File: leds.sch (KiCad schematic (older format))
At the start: 0 parts

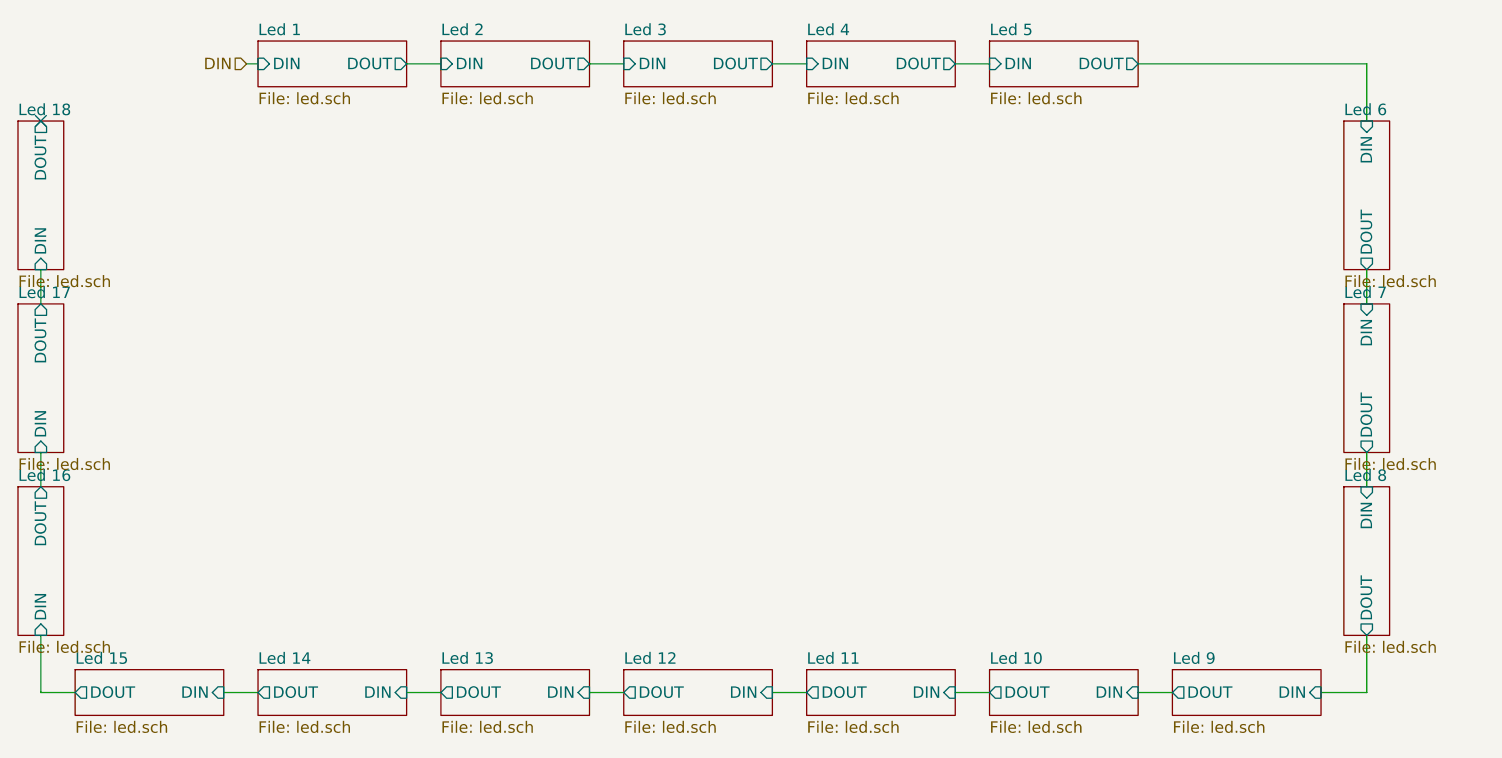
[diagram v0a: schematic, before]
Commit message: Place and route WS2812 LEDs
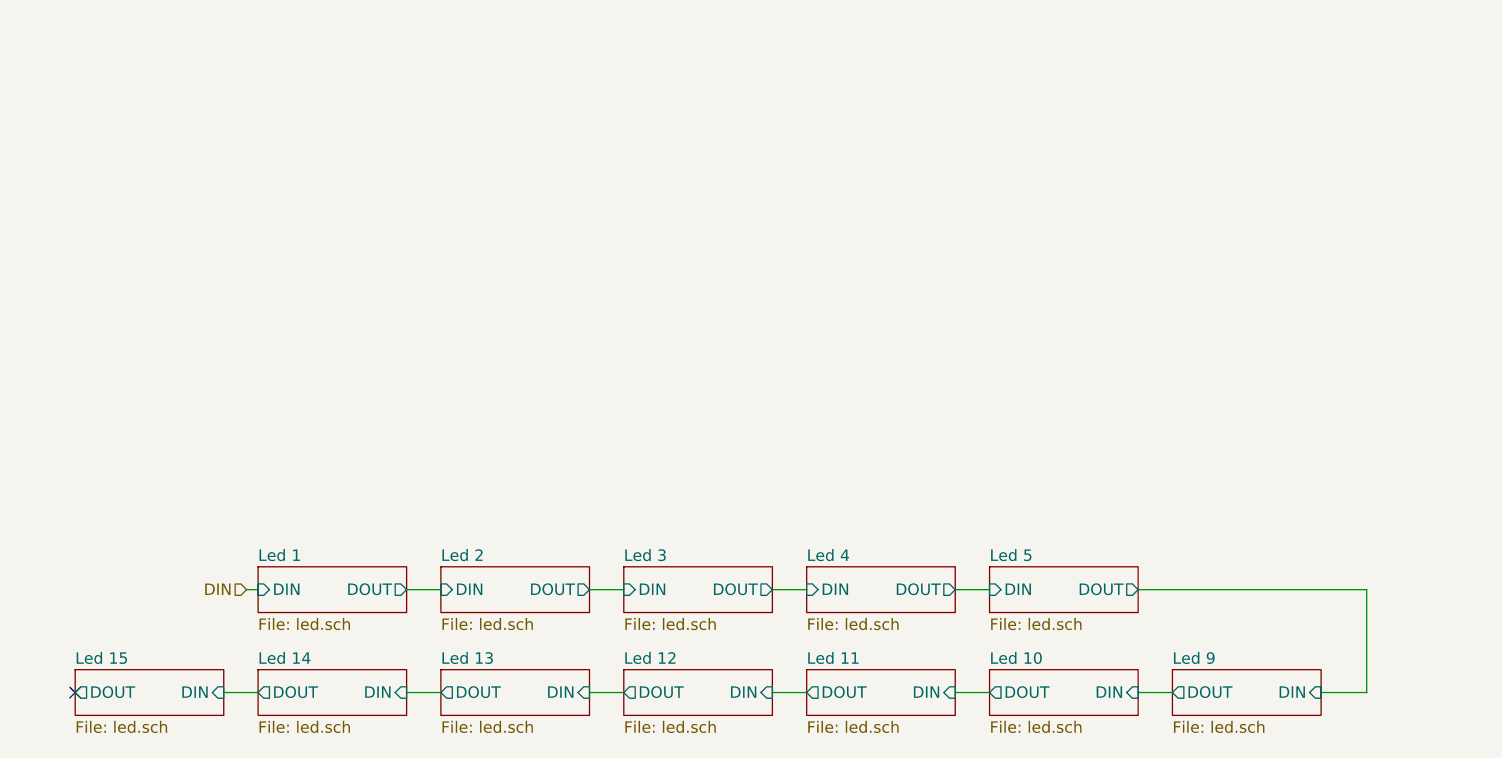
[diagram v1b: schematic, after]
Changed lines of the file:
@@
 $Descr A4 11693 8268
 encoding utf-8
-Sheet 5 23
+Sheet 5 17
 Title ""
 Date ""
@@
 Comment4 ""
 $EndDescr
-Text HLabel 2450 2200 0    50   Input ~ 0
+Text HLabel 2450 4500 0    50   Input ~ 0
 DIN
-$Sheet
-S 7250 2450 200  650
-U 620616BF
-F0 "Led 6" 50
-F1 "led.sch" 50
-F2 "DIN" I T 7350 2450 50
-F3 "DOUT" O B 7350 3100 50
-$EndSheet
-Wire Wire Line
-	7350 3100 7350 3250
-Wire Wire Line
-	7350 2450 7350 2200
-$Sheet
-S 7250 3250 200  650
-U 6206183F
-F0 "Led 7" 50
-F1 "led.sch" 50
-F2 "DIN" I T 7350 3250 50
-F3 "DOUT" O B 7350 3900 50
-$EndSheet
-Wire Wire Line
-	7350 3900 7350 4050
-$Sheet
-S 7250 4050 200  650
-U 62061912
-F0 "Led 8" 50
-F1 "led.sch" 50
-F2 "DIN" I T 7350 4050 50
-F3 "DOUT" O B 7350 4700 50
-$EndSheet
 $Sheet
 S 6500 4850 650  200
@@
 Wire Wire Line
 	7150 4950 7350 4950
-Wire Wire Line
-	7350 4700 7350 4950
 Wire Wire Line
 	5700 4950 5550 4950
@@
 F3 "DOUT" O L 1700 4950 50
 $EndSheet
-Wire Wire Line
-	1700 4950 1550 4950
-$Sheet
-S 1450 4050 200  650
-U 62062FE6
-F0 "Led 16" 50
-F1 "led.sch" 50
-F2 "DIN" I B 1550 4700 50
-F3 "DOUT" O T 1550 4050 50
-$EndSheet
-Wire Wire Line
-	1550 4050 1550 3900
-Wire Wire Line
-	1550 4700 1550 4950
-$Sheet
-S 1450 3250 200  650
-U 62063495
-F0 "Led 17" 50
-F1 "led.sch" 50
-F2 "DIN" I B 1550 3900 50
-F3 "DOUT" O T 1550 3250 50
-$EndSheet
-Wire Wire Line
-	1550 3250 1550 3100
-$Sheet
-S 1450 2450 200  650
-U 620637A1
-F0 "Led 18" 50
-F1 "led.sch" 50
-F2 "DIN" I B 1550 3100 50
-F3 "DOUT" O T 1550 2450 50
-$EndSheet
-NoConn ~ 1550 2450
 $Sheet
 S 5700 4850 650  200
@@
 $EndSheet
 $Sheet
-S 5700 2100 650  200
+S 5700 4400 650  200
 U 62060D3F
 F0 "Led 5" 50
 F1 "led.sch" 50
-F2 "DIN" I L 5700 2200 50
-F3 "DOUT" O R 6350 2200 50
+F2 "DIN" I L 5700 4500 50
+F3 "DOUT" O R 6350 4500 50
 $EndSheet
 Wire Wire Line
-	5550 2200 5700 2200
+	5550 4500 5700 4500
 $Sheet
-S 4900 2100 650  200
+S 4900 4400 650  200
 U 62060CAF
 F0 "Led 4" 50
 F1 "led.sch" 50
-F2 "DIN" I L 4900 2200 50
-F3 "DOUT" O R 5550 2200 50
+F2 "DIN" I L 4900 4500 50
+F3 "DOUT" O R 5550 4500 50
 $EndSheet
 Wire Wire Line
-	4750 2200 4900 2200
+	4750 4500 4900 4500
 $Sheet
-S 4100 2100 650  200
+S 4100 4400 650  200
 U 62060C37
 F0 "Led 3" 50
 F1 "led.sch" 50
-F2 "DIN" I L 4100 2200 50
-F3 "DOUT" O R 4750 2200 50
+F2 "DIN" I L 4100 4500 50
+F3 "DOUT" O R 4750 4500 50
 $EndSheet
 Wire Wire Line
-	3950 2200 4100 2200
+	3950 4500 4100 4500
 $Sheet
-S 3300 2100 650  200
+S 3300 4400 650  200
 U 62060AD8
 F0 "Led 2" 50
 F1 "led.sch" 50
-F2 "DIN" I L 3300 2200 50
-F3 "DOUT" O R 3950 2200 50
+F2 "DIN" I L 3300 4500 50
+F3 "DOUT" O R 3950 4500 50
 $EndSheet
 Wire Wire Line
-	3150 2200 3300 2200
+	3150 4500 3300 4500
 Wire Wire Line
-	2500 2200 2450 2200
+	2500 4500 2450 4500
 $Sheet
-S 2500 2100 650  200
+S 2500 4400 650  200
 U 6205EA4D
 F0 "Led 1" 50
 F1 "led.sch" 50
-F2 "DIN" I L 2500 2200 50
-F3 "DOUT" O R 3150 2200 50
+F2 "DIN" I L 2500 4500 50
+F3 "DOUT" O R 3150 4500 50
 $EndSheet
 Wire Wire Line
-	6350 2200 7350 2200
+	6350 4500 7350 4500
+Wire Wire Line
+	7350 4500 7350 4950
+NoConn ~ 1700 4950
 $EndSCHEMATC
